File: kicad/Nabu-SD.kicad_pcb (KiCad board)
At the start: 2 copper layers, 80.2 x 56.5 mm, 22 parts, among them J1 Nabu Expansion Slot, J2 ICSP, J3 SD Card, J4 Serial, J5 I2C, J6 OUT1, U1 PIC18F47Q84-E/P, U2 DS1307N+, Y1 32KHz

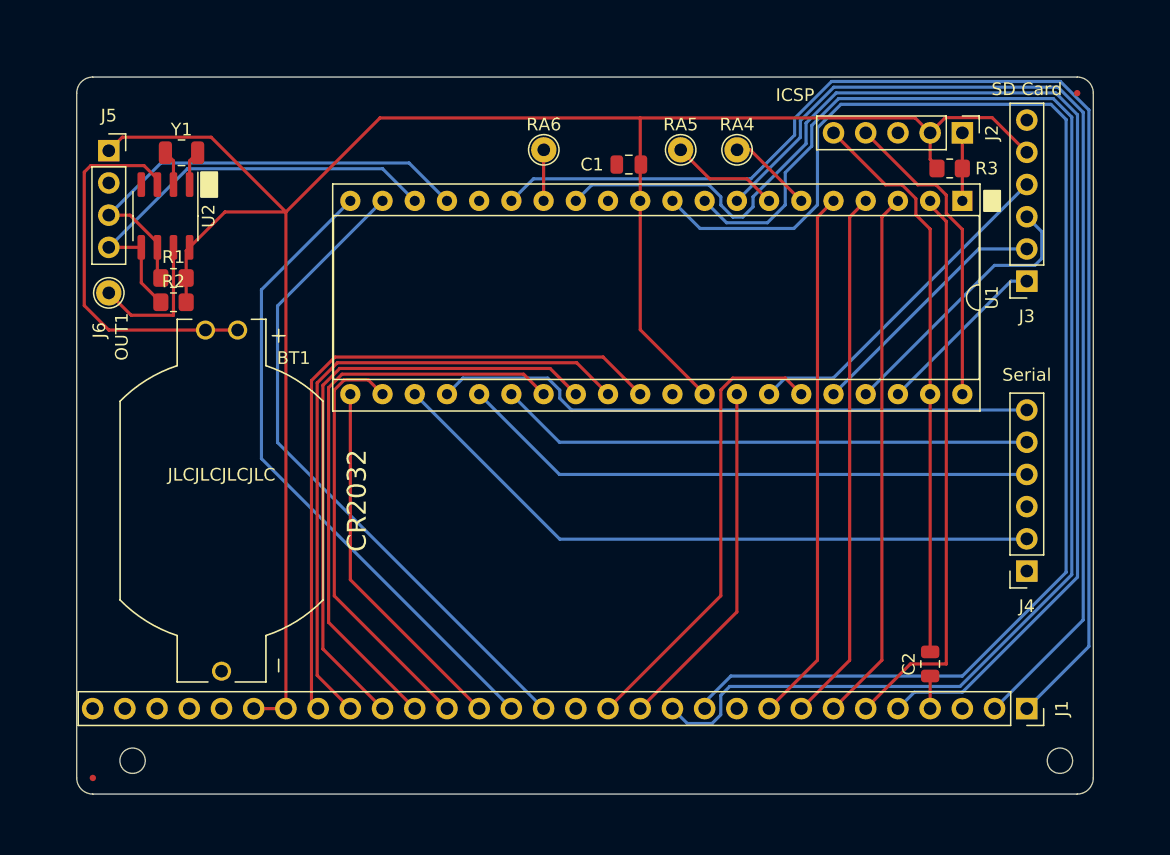
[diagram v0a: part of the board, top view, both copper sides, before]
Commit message: Corrected 1 resistor value; Added a Solder Jumper to close AFTER flashing PIC. Reduced the size of the board.  Moved to mostly SMD parts (where possible).
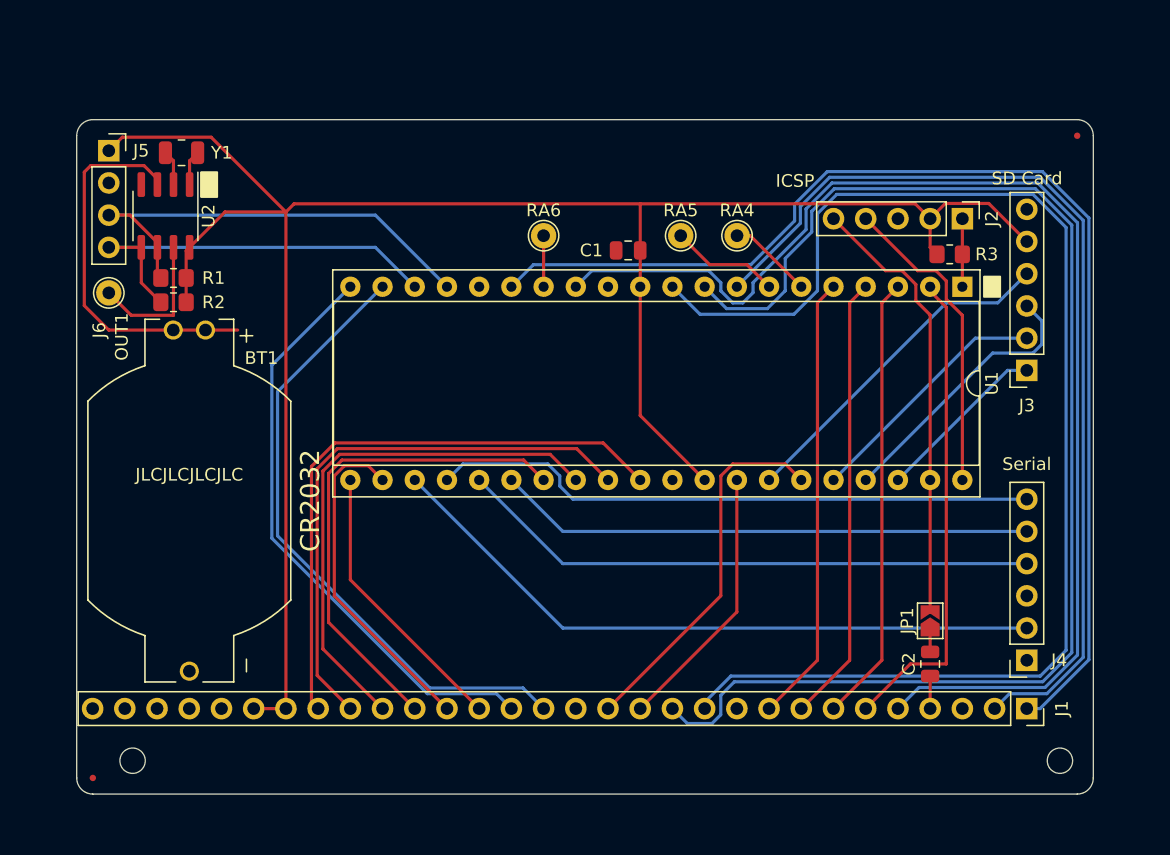
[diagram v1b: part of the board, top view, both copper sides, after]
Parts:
- added JP1: ICSP Close, Jumper:SolderJumper-2_P1.3mm_Open_TrianglePad1.0x1.5mm, F.Cu at (94.0, 118.4)
- R3: value 60K -> 10K
- moved J3 7.03 mm to (101.6, 98.7)
- moved J4 7.03 mm to (101.6, 121.5)
- moved C1 6.77 mm to (70.2, 89.2)
- moved RA6 6.77 mm to (63.5, 88.0)
- moved J2 6.77 mm to (96.5, 86.7)
- moved R3 6.77 mm to (95.5, 89.5)
- moved RA4 6.77 mm to (78.7, 88.0)
- moved RA5 6.77 mm to (74.3, 88.0)
- moved U1 6.77 mm to (96.5, 92.1)
- moved REF1 3.36 mm to (105.6, 80.2)
- moved BT1 2.54 mm to (35.5, 108.9)
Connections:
- C2 pad 2: /RB6 -> Net-(C2-Pad2)
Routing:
- net /RB6: track 44.9 -> 34.9 mm
- net //INT: track 100.4 -> 92.9 mm
- net /D6: track 51.4 -> 44.6 mm
- net /D5: track 48.8 -> 42.0 mm
- net /A3: track 42.1 -> 35.4 mm
- net //WAIT: track 36.1 -> 29.3 mm
- net //IORQ: track 28.0 -> 21.2 mm
- net /D7: track 54.0 -> 47.2 mm
- net /D4: track 46.2 -> 39.4 mm
- net /D3: track 33.4 -> 26.6 mm
- net /D2: track 29.0 -> 22.2 mm
- net /A2: track 42.1 -> 35.4 mm
- net /A1: track 42.1 -> 35.4 mm
- net /A0: track 44.9 -> 38.1 mm
- net //M1: track 82.5 -> 76.2 mm
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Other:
- board size 80.2 x 56.5 mm -> 80.2 x 53.2 mm

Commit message: This Project uses CR2032 vs CR1220; Added README; Updated silkscreen; Added missing KiCAD project file.
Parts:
- moved REF4 4.12 mm to (100.1, 129.4)
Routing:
- net /VBAT: track 30.0 -> 27.5 mm
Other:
- outline, holes or cut-outs redrawn
- board text added: "Original design by Ken {dblquote}The Codeman{dblquote} Segler: https://www.youtube.com/@kensegler https://github.com/TheCodeman"
- board text added: "SD Card Expansion & More!"
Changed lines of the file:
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@@
   )
   (footprint "MountingHole:MountingHole_2mm" (layer "F.Cu")
-    (at 104.2 129.45)
+    (at 100.08 129.45)
     (descr "Mounting Hole 2mm, no annular")
     (tags "mounting hole 2mm no annular")
@@
   (gr_rect (start 36.475 83.045) (end 37.745 84.995) (layer "F.SilkS") (width 0.15) (fill solid))
   (gr_rect (start 98.215 91.275) (end 99.485 92.875) (layer "F.SilkS") (width 0.15) (fill solid))
-  (gr_line (start 27.94 132.08) (end 105.56 132.08) (layer "Edge.Cuts") (width 0.1))
+  (gr_line (start 27.94 132.08) (end 101.44 132.08) (layer "Edge.Cuts") (width 0.1))
   (gr_arc (start 27.94 132.08) (mid 27.042004 131.707996) (end 26.67 130.81) (layer "Edge.Cuts") (width 0.1))
-  (gr_line (start 106.83 80.17) (end 106.83 130.81) (layer "Edge.Cuts") (width 0.1))
+  (gr_line (start 106.83 80.17) (end 106.83 125.73) (layer "Edge.Cuts") (width 0.1))
   (gr_line (start 26.67 80.17) (end 26.67 130.81) (layer "Edge.Cuts") (width 0.1))
+  (gr_arc (start 106.83 125.73) (mid 106.458026 126.628026) (end 105.56 127) (layer "Edge.Cuts") (width 0.1))
+  (gr_line (start 103.98 127) (end 105.56 127) (layer "Edge.Cuts") (width 0.1))
   (gr_arc (start 105.56 78.9) (mid 106.458055 79.271945) (end 106.83 80.17) (layer "Edge.Cuts") (width 0.1))
-  (gr_arc (start 106.83 130.81) (mid 106.458026 131.708026) (end 105.56 132.08) (layer "Edge.Cuts") (width 0.1))
+  (gr_arc (start 102.71 130.81) (mid 102.338026 131.708026) (end 101.44 132.08) (layer "Edge.Cuts") (width 0.1))
+  (gr_line (start 102.71 128.27) (end 102.71 130.81) (layer "Edge.Cuts") (width 0.1))
+  (gr_arc (start 102.71 128.27) (mid 103.081974 127.371974) (end 103.98 127) (layer "Edge.Cuts") (width 0.1))
   (gr_line (start 27.94 78.9) (end 105.56 78.9) (layer "Edge.Cuts") (width 0.1))
   (gr_arc (start 26.67 80.17) (mid 27.041974 79.271974) (end 27.94 78.9) (layer "Edge.Cuts") (width 0.1))
+  (gr_text "Original design by Ken {dblquote}The Codeman{dblquote} Segler: \nhttps://www.youtube.com/@kensegler\nhttps://github.com/TheCodeman" (at 40.5 121.5) (layer "F.SilkS")
+    (effects (font (size 0.8 0.8) (thickness 0.1)) (justify left))
+  )
   (gr_text "CR2032" (at 45.085 108.94 90) (layer "F.SilkS")
     (effects (font (size 1.5 1.5) (thickness 0.3)))
@@
   (gr_text "JLCJLCJLCJLC" (at 35.55 106.9) (layer "F.SilkS")
     (effects (font (size 1 1) (thickness 0.15)))
+  )
+  (gr_text "SD Card Expansion\n  & More!" (at 41 84.5) (layer "F.SilkS")
+    (effects (font (size 2.5 2.5) (thickness 0.5)) (justify left))
   )
   (segment (start 93.965 92.075) (end 93.965 92.421396) (width 0.25) (layer "F.Cu") (net 1))
@@
   (segment (start 33.665 81.51) (end 34.3 82.145) (width 0.25) (layer "F.Cu") (net 39))
   (segment (start 34.3 82.145) (end 34.3 84.02) (width 0.25) (layer "F.Cu") (net 39))
+  (segment (start 27.776352 82.525) (end 31.976751 82.525) (width 0.25) (layer "F.Cu") (net 40))
+  (segment (start 29.196 95.49) (end 27.265 93.559) (width 0.25) (layer "F.Cu") (net 40))
+  (segment (start 31.976751 82.525) (end 33.03 83.578249) (width 0.25) (layer "F.Cu") (net 40))
+  (segment (start 27.265 83.036352) (end 27.776352 82.525) (width 0.25) (layer "F.Cu") (net 40))
+  (segment (start 36.82 95.49) (end 29.196 95.49) (width 0.25) (layer "F.Cu") (net 40))
   (segment (start 27.265 93.559) (end 27.265 83.036352) (width 0.25) (layer "F.Cu") (net 40))
-  (segment (start 27.265 83.036352) (end 27.776352 82.525) (width 0.25) (layer "F.Cu") (net 40))
-  (segment (start 27.776352 82.525) (end 31.976751 82.525) (width 0.25) (layer "F.Cu") (net 40))
-  (segment (start 39.36 95.49) (end 29.196 95.49) (width 0.25) (layer "F.Cu") (net 40))
   (segment (start 33.03 83.578249) (end 33.03 83.795) (width 0.25) (layer "F.Cu") (net 40))
-  (segment (start 31.976751 82.525) (end 33.03 83.578249) (width 0.25) (layer "F.Cu") (net 40))
-  (segment (start 29.196 95.49) (end 27.265 93.559) (width 0.25) (layer "F.Cu") (net 40))
   (segment (start 34.3 88.97) (end 34.3 94.325) (width 0.25) (layer "F.Cu") (net 41))
   (segment (start 34.3 94.325) (end 30.965 94.325) (width 0.25) (layer "F.Cu") (net 41))

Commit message: Created the SD Card and Serial Card breakouts and included them in schematic. Prettied up all of the 3D Models and rendered them in the board view. Added all used external models, footprints, and symbols.
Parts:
- added C3: 10uF, Capacitor_SMD:C_0805_2012Metric_Pad1.18x1.45mm_HandSolder, F.Cu at (146.2, 42.5)
- added C4: 0.1uF, Capacitor_SMD:C_0805_2012Metric_Pad1.18x1.45mm_HandSolder, F.Cu at (155.2, 42.0)
- added C5: 10uF, Capacitor_SMD:C_0805_2012Metric_Pad1.18x1.45mm_HandSolder, F.Cu at (156.1, 36.7)
- added C6: 0.1uF, Capacitor_SMD:C_0805_2012Metric_Pad1.18x1.45mm_HandSolder, F.Cu at (154.2, 45.9)
- added C7: 0.1uF, Capacitor_SMD:C_0805_2012Metric_Pad1.18x1.45mm_HandSolder, F.Cu at (150.3, 64.1)
- added C8: 10uF, Capacitor_SMD:C_0805_2012Metric_Pad1.18x1.45mm_HandSolder, F.Cu at (153.3, 63.0)
- added C9: 0.1uF, Capacitor_SMD:C_0805_2012Metric_Pad1.18x1.45mm_HandSolder, F.Cu at (155.3, 63.0)
- added D1R1: TX_RED, LED_SMD:LED_0805_2012Metric_Pad1.15x1.40mm_HandSolder, F.Cu at (167.6, 64.0)
- added D2G1: RX_GREEN, LED_SMD:LED_0805_2012Metric_Pad1.15x1.40mm_HandSolder, F.Cu at (167.6, 76.0)
- added DCD: TestPoint_THTPad_D2.0mm_Drill1.0mm, TestPoint:TestPoint_THTPad_D2.0mm_Drill1.0mm, F.Cu at (148.8, 78.0)
- added DCR: TestPoint_THTPad_D2.0mm_Drill1.0mm, TestPoint:TestPoint_THTPad_D2.0mm_Drill1.0mm, F.Cu at (153.9, 78.0)
- added F1: MF-NSHT010KX-2, Fuse:Fuse_1206_3216Metric_Pad1.42x1.75mm_HandSolder, F.Cu at (159.0, 64.0)
- added J10: USB_B_Micro, Nabu-SD:CUI_UJ2-MIBH-4-SMT, F.Cu at (161.8, 71.3)
- added J7: SD Card, Connector_PinHeader_2.54mm:PinHeader_1x06_P2.54mm_Vertical, F.Cu at (131.7, 52.2)
- added J8A1: XKTF-005, Nabu-SD:TF-SMD_XKTF-005, F.Cu at (163.4, 45.9)
- added J8B1: XKTF-0803-0, Nabu-SD:TF-SMD_XKTF-0803-0, F.Cu at (164.3, 45.9)
- added J9: Serial, Connector_PinHeader_2.54mm:PinHeader_1x06_P2.54mm_Vertical, F.Cu at (131.7, 76.3)
- added R4: 3.3K, Resistor_SMD:R_0805_2012Metric_Pad1.20x1.40mm_HandSolder, F.Cu at (143.2, 47.2)
- added R5: 3.3K, Resistor_SMD:R_0805_2012Metric_Pad1.20x1.40mm_HandSolder, F.Cu at (143.2, 49.7)
- added R6: 3.3K, Resistor_SMD:R_0805_2012Metric_Pad1.20x1.40mm_HandSolder, F.Cu at (143.2, 52.2)
- added R7: 3.3K, Resistor_SMD:R_0805_2012Metric_Pad1.20x1.40mm_HandSolder, F.Cu at (164.1, 53.8)
- added R8: 330, Resistor_SMD:R_0805_2012Metric_Pad1.20x1.40mm_HandSolder, F.Cu at (158.5, 61.8)
- added R9: 330, Resistor_SMD:R_0805_2012Metric_Pad1.20x1.40mm_HandSolder, F.Cu at (162.1, 76.0)
- added REF**: MountingHole_2.2mm_M2_ISO7380, MountingHole:MountingHole_2.2mm_M2_ISO7380, F.Cu at (167.6, 55.9)
- added REF**: MountingHole_2.2mm_M2_ISO7380, MountingHole:MountingHole_2.2mm_M2_ISO7380, F.Cu at (167.6, 80.0)
- added REF**: MountingHole_2.2mm_M2_ISO7380, MountingHole:MountingHole_2.2mm_M2_ISO7380, F.Cu at (125.6, 80.0)
- added REF**: MountingHole_2.2mm_M2_ISO7380, MountingHole:MountingHole_2.2mm_M2_ISO7380, F.Cu at (167.6, 60.0)
- added REF**: MountingHole_2.2mm_M2_ISO7380, MountingHole:MountingHole_2.2mm_M2_ISO7380, F.Cu at (129.7, 80.0)
- added REF**: MountingHole_2.2mm_M2_ISO7380, MountingHole:MountingHole_2.2mm_M2_ISO7380, F.Cu at (167.6, 35.9)
- added REF**: MountingHole_2.2mm_M2_ISO7380, MountingHole:MountingHole_2.2mm_M2_ISO7380, F.Cu at (129.7, 60.0)
- added REF**: TestPoint_Pad_D1.0mm, TestPoint:TestPoint_Pad_D1.0mm, F.Cu at (143.2, 54.3)
- added REF**: MountingHole_2.2mm_M2_ISO7380, MountingHole:MountingHole_2.2mm_M2_ISO7380, F.Cu at (129.7, 35.9)
- added REF**: MountingHole_2.2mm_M2_ISO7380, MountingHole:MountingHole_2.2mm_M2_ISO7380, F.Cu at (129.7, 55.9)
- added REF**: MountingHole_2.2mm_M2_ISO7380, MountingHole:MountingHole_2.2mm_M2_ISO7380, F.Cu at (125.6, 60.0)
- added REF**: MountingHole_2.2mm_M2_ISO7380, MountingHole:MountingHole_2.2mm_M2_ISO7380, F.Cu at (125.6, 35.9)
- added REF**: MountingHole_2.2mm_M2_ISO7380, MountingHole:MountingHole_2.2mm_M2_ISO7380, F.Cu at (125.6, 55.9)
- added RTS: TestPoint_THTPad_D2.0mm_Drill1.0mm, TestPoint:TestPoint_THTPad_D2.0mm_Drill1.0mm, F.Cu at (139.7, 66.2)
- added U3: 74LVC125, Package_SO:TSSOP-14_4.4x5mm_P0.65mm, F.Cu at (150.7, 49.7)
- added U4: LM1117-3.3, Nabu-SD:SOT-223, F.Cu at (150.7, 39.9)
- added U5: FT232RL, Package_SO:SSOP-28_5.3x10.2mm_P0.65mm, F.Cu at (148.6, 70.0)
- BT1: value BU2032-1 -> BU2032-1-HD-G
- C1, C2: footprint Capacitor_SMD:C_0805_2012Metric -> Capacitor_SMD:C_0805_2012Metric_Pad1.18x1.45mm_HandSolder
- JP1: value ICSP Close -> ICSP Disable; footprint Jumper:SolderJumper-2_P1.3mm_Open_TrianglePad1.0x1.5mm -> Connector_PinHeader_2.54mm:PinHeader_1x02_P2.54mm_Horizontal
- Y1: footprint Nabu-SD:SMD3215-2P -> Nabu-SD:XTAL_ECS-.327-12.5-34B
- moved J3 49.1 mm to (117.6, 52.2)
- moved JP1 48.6 mm to (110.0, 72.5), turned to 180 degrees
- moved C2 48.1 mm to (110.0, 76.4)
- moved REF1 48.0 mm to (122.3, 35.2)
- moved J4 47.9 mm to (117.6, 76.3)
- moved R1 47.8 mm to (50.3, 46.4)
- moved U2 47.8 mm to (49.7, 41.5)
- moved BT1 47.8 mm to (51.5, 63.9)
- moved J1 47.8 mm to (117.6, 80.3)
- moved J6 47.8 mm to (45.2, 47.6)
- moved R2 47.8 mm to (50.3, 48.3)
- moved RA4 47.8 mm to (94.7, 43.0)
- moved RA5 47.8 mm to (90.3, 43.0)
- moved RA6 47.8 mm to (79.5, 43.0)
- moved REF2 47.8 mm to (43.9, 85.8)
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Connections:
- net /SCK2 renamed /SPISCK
- net /SDI2 renamed /MISO
- net /SDO2 renamed /MOSI
- J4 pad 3: unconnected-(J4-Pad3) -> +5VD
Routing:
- net GND: track 0.00 -> 162.3 mm, vias 0 -> 1
- net +5VD: track 0.00 -> 124.4 mm
- net +3V3: track 0.00 -> 47.6 mm
- net /MicroSD_Breakout/SD_SSEL: track 0.00 -> 38.1 mm, vias 0 -> 2
- net +5V: track 159.6 -> 192.5 mm
- net /Serial_Breakout/TXLED_RED: track 0.00 -> 24.6 mm
- net /Serial_Breakout/RXLED_GRN: track 0.00 -> 24.6 mm
- net /MISO: track 27.1 -> 51.6 mm
- net /MicroSD_Breakout/SD_MOSI: track 0.00 -> 23.8 mm, vias 0 -> 3
- net /MicroSD_Breakout/SD_CLK: track 0.00 -> 23.7 mm, vias 0 -> 2
- net /RC4: track 53.1 -> 74.6 mm
- net /RX1: track 45.9 -> 65.9 mm
- net /Serial_Breakout/USBDATA1: track 0.00 -> 18.6 mm
- net /RC5: track 47.9 -> 66.2 mm
- net /TX1: track 42.3 -> 58.1 mm
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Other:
- board size 80.2 x 53.2 mm -> 127 x 53.2 mm
- board text added: "+5V"
- board text added: "CTS"
- board text added: "Clock OUT1"
- board text added: "Current iteration available via: https://github.com/ayourk/ Nabu-SD/tree/main/kicad"
- board text added: "DTR"
- board text added: "GND"
- board text added: "MISO"
- board text added: "MOSI"
- board text added: "MicroSD"
- board text added: "Note: MicroSD holder could be changed to XKTF-0803-0 (C381083)"
- board text added: "RECV"
- board text added: "SCK"
- board text added: "SCL"
- board text added: "SD Card Breakout"
- board text added: "SDA"
- board text added: "SD_CS"
- board text added: "SEND"
- board text added: "Serial Breakout"
- board text added: "card size"
- board text added: "for SD Card Expansion & More!"
